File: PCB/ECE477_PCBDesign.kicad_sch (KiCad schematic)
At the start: 0 parts

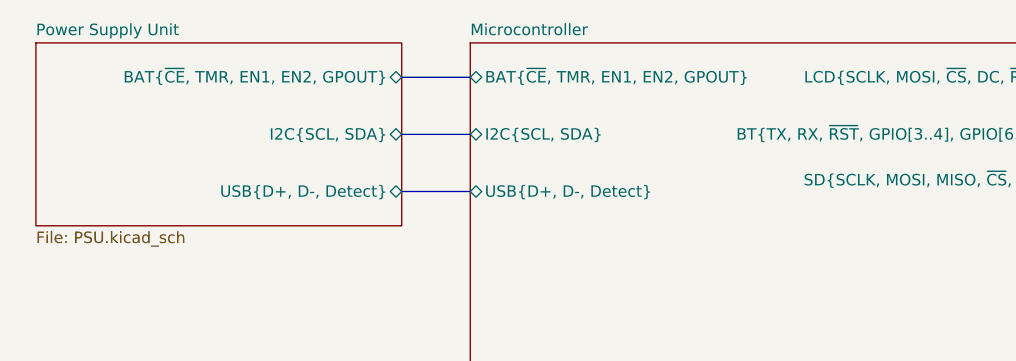
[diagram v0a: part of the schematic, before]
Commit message: Redesign bluetooth of v2
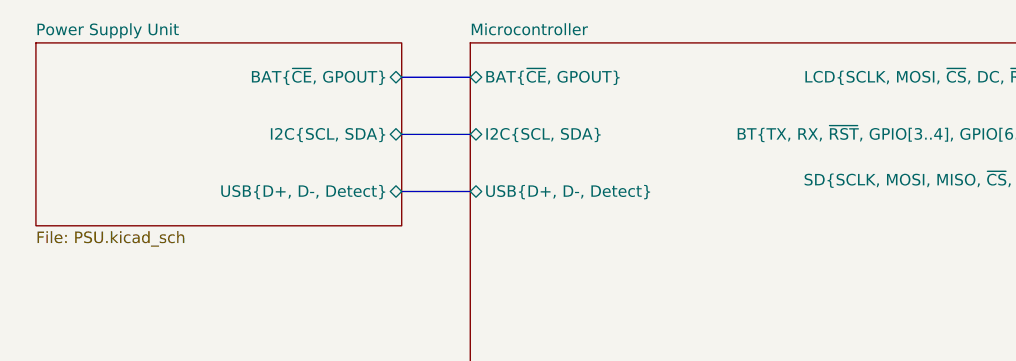
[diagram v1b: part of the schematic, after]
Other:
- sheet Microcontroller ports: added BAT{~{CE}, GPOUT}; removed BAT{~{CE}, TMR, EN1, EN2, GPOUT}
- sheet Power Supply Unit ports: added BAT{~{CE}, GPOUT}; removed BAT{~{CE}, TMR, EN1, EN2, GPOUT}
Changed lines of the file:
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@@
       (effects (font (size 1.27 1.27)) (justify right))
     )
-    (pin "BAT{~{CE}, TMR, EN1, EN2, GPOUT}" bidirectional (at 162.56 118.11 0)
+    (pin "BAT{~{CE}, GPOUT}" bidirectional (at 162.56 118.11 0)
       (effects (font (size 1.27 1.27)) (justify right))
     )
@@
       (effects (font (size 1.27 1.27)) (justify right))
     )
-    (pin "BAT{~{CE}, TMR, EN1, EN2, GPOUT}" bidirectional (at 170.18 118.11 180)
-      (effects (font (size 1.27 1.27)) (justify left))
-    )
     (pin "LCD{SCLK, MOSI, ~{CS}, DC, ~{RST}}" bidirectional (at 236.22 118.11 0)
       (effects (font (size 1.27 1.27)) (justify right))
@@
       (effects (font (size 1.27 1.27)) (justify right))
     )
+    (pin "BAT{~{CE}, GPOUT}" bidirectional (at 170.18 118.11 180)
+      (effects (font (size 1.27 1.27)) (justify left))
+    )
     (instances
